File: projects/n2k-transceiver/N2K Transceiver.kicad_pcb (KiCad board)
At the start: 4 copper layers, 60 x 75 mm, 83 parts, among them J1 JTAG, SW1 SW_MEC_5G, SW2 SW_MEC_5G, SW3 SW_MEC_5G, SW4 SW_MEC_5G

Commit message: Progressing on new N2K Transceiver PCB layout
Signed-off-by: digimer <digital.mermaid@gmail.com>
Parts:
- removed C64, C65: 0.1uF, mr-stuff:Kyocera AVX 0805
- removed R24: 10kR, mr-stuff:Stackpole_RNCP1206
- removed R52: 475R, mr-stuff:Stackpole RNCP0805
- removed SW4: SW_MEC_5G, mr-stuff:SW_TS03-66-50-BK-160-LCR-D-67
- added C15: C, mr-stuff:Kyocera AVX 0805, F.Cu at (274.0, -40.7)
- added C18: C, mr-stuff:Kyocera AVX 0805, F.Cu at (230.2, -37.6)
- added C20: 0.1uF, mr-stuff:Kyocera AVX 0805, F.Cu at (125.5, 54.8)
- added C21: 0.1uF, mr-stuff:Kyocera AVX 0805, F.Cu at (172.5, 49.1)
- added C22: 0.1uF, mr-stuff:Kyocera AVX 0805, F.Cu at (172.5, 51.3)
- added C23: 0.1uF, mr-stuff:Kyocera AVX 0805, F.Cu at (172.5, 59.1)
- added C24: 0.1uF, mr-stuff:Kyocera AVX 0805, F.Cu at (172.5, 61.3)
- added C25: 0.1uF, mr-stuff:Kyocera AVX 0805, F.Cu at (205.8, 68.7)
- added C26: 0.1uF, mr-stuff:Kyocera AVX 0805, F.Cu at (205.8, 71.8)
- added C27: 0.1uF, mr-stuff:Kyocera AVX 0805, F.Cu at (205.7, 78.9)
- added C28: 0.1uF, mr-stuff:Kyocera AVX 0805, F.Cu at (205.7, 82.0)
- added C29: 0.1uF, mr-stuff:Kyocera AVX 0805, F.Cu at (205.9, 93.9)
- added C30: 0.1uF, mr-stuff:Kyocera AVX 0805, F.Cu at (205.9, 97.0)
- added C31: 0.1uF, mr-stuff:Kyocera AVX 0805, F.Cu at (205.6, 110.6)
- added HDR1: 0022112032, mr-stuff:Molex 0022112032, F.Cu at (192.5, 50.8)
- added HDR2: 0022112032, mr-stuff:Molex 0022112032, F.Cu at (192.5, 60.8)
- added HDR3: 0022112032, mr-stuff:Molex 0022112032, F.Cu at (192.5, 70.8)
- added HDR4: 0022112032, mr-stuff:Molex 0022112032, F.Cu at (192.5, 80.8)
- added HDR5: 0022112032, mr-stuff:Molex 0022112032, F.Cu at (192.5, 90.8)
- added HDR6: 0022112032, mr-stuff:Molex 0022112032, F.Cu at (192.5, 100.8)
- added HDR7: 0022112032, mr-stuff:Molex 0022112032, F.Cu at (192.5, 110.8)
- added IOX1: PI4IOE5V6416RQ2LEX, mr-stuff:Diodes Inc PI4IOE5V6416RQ2LEX, F.Cu at (249.9, 19.3)
- added R29: 475R, mr-stuff:Stackpole RNCP0805, F.Cu at (178.0, 47.1)
- added R30: 4.7kR, mr-stuff:Stackpole RMCA0805, F.Cu at (172.5, 47.1)
- added R31: 475R, mr-stuff:Stackpole RNCP0805, F.Cu at (178.0, 49.1)
- added R32: 4.7kR, mr-stuff:Stackpole RMCA0805, F.Cu at (172.5, 53.4)
- added R33: 475R, mr-stuff:Stackpole RNCP0805, F.Cu at (178.0, 57.1)
- added R34: 4.7kR, mr-stuff:Stackpole RMCA0805, F.Cu at (172.5, 57.1)
- added R35: 475R, mr-stuff:Stackpole RNCP0805, F.Cu at (178.0, 59.1)
- added R36: 4.7kR, mr-stuff:Stackpole RMCA0805, F.Cu at (172.5, 63.4)
- added R37: 475R, mr-stuff:Stackpole RNCP0805, F.Cu at (209.9, 69.3)
- added R38: 4.7kR, mr-stuff:Stackpole RMCA0805, F.Cu at (214.1, 69.1)
- added R39: 475R, mr-stuff:Stackpole RNCP0805, F.Cu at (209.8, 71.4)
- added R40: 4.7kR, mr-stuff:Stackpole RMCA0805, F.Cu at (214.1, 72.2)
- added R41: 475R, mr-stuff:Stackpole RNCP0805, F.Cu at (209.8, 79.0)
- added R42: 4.7kR, mr-stuff:Stackpole RMCA0805, F.Cu at (213.9, 79.2)
- added R43: 475R, mr-stuff:Stackpole RNCP0805, F.Cu at (209.8, 82.0)
- added R44: 4.7kR, mr-stuff:Stackpole RMCA0805, F.Cu at (213.9, 82.0)
- added R45: 475R, mr-stuff:Stackpole RNCP0805, F.Cu at (209.9, 93.9)
- added R46: 4.7kR, mr-stuff:Stackpole RMCA0805, F.Cu at (214.0, 93.9)
- added R47: 475R, mr-stuff:Stackpole RNCP0805, F.Cu at (209.9, 96.9)
- added R48: 4.7kR, mr-stuff:Stackpole RMCA0805, F.Cu at (214.0, 97.0)
- added R49: 10kR, mr-stuff:Stackpole RNCP0805, F.Cu at (234.0, -18.1)
- added R50: 10kR, mr-stuff:Stackpole RNCP0805, F.Cu at (234.0, -15.1)
- added R55: 475R, mr-stuff:Stackpole RNCP0805, F.Cu at (212.9, 110.6)
- added R57: 4.7kR, mr-stuff:Stackpole RMCA0805, F.Cu at (209.4, 110.6)
- added TVS4: TPD2E2U06QDBZRQ1, mr-stuff:TI TPD2E2U06, F.Cu at (184.0, 48.1)
- added TVS5: TPD2E2U06QDBZRQ1, mr-stuff:TI TPD2E2U06, F.Cu at (184.0, 58.1)
- added TVS6: TPD2E2U06QDBZRQ1, mr-stuff:TI TPD2E2U06, F.Cu at (201.5, 70.4)
- added TVS7: TPD2E2U06QDBZRQ1, mr-stuff:TI TPD2E2U06, F.Cu at (201.4, 80.0)
- added TVS8: TPD2E2U06QDBZRQ1, mr-stuff:TI TPD2E2U06, F.Cu at (201.5, 95.4)
- added TVS9: TPD2E2U06QDBZRQ1, mr-stuff:TI TPD2E2U06, F.Cu at (201.2, 110.6)
- C1, C12, C16, C17, C4: value 0.1uF -> C
- C10, C2, C3: value 10uF -> C
- C11, C14, C9: value 1uF -> C
- C7, C8: value 22uF -> C
- CMC1: value ACT12101012PTL00 -> ACT1210-101-2P-TL00
- H1, H2, H3, H4: value MountingHole_Pad -> MountingHole
- J1: value JTAG -> Conn_01x05_Pin
- LED1, LED2, LED3, LED4, LED5, LED6, LED7: value LED -> TLMS1101-GS15; footprint mr-stuff:ams OSRAM LS Q976.01 -> mr-stuff:Vishay TLMS1101
- R1, R10, R11, R12, R13, R17, R18, R2, R8, R9: footprint mr-stuff:Stackpole_RNCP1206 -> mr-stuff:Stackpole RNCP0805
- R14: value 15kR -> R
- R15, R16: value 5.11kR -> R
- R19, R20: value 10kR -> 4.7kR; footprint mr-stuff:Stackpole_RNCP1206 -> mr-stuff:Stackpole RMCA0805
- R3, R4, R7: value 0R -> RCA08050000ZSEASR
- R5: value 470kR -> R
- R6: value 100kR -> R
- ROM1, ROM2: value M24C64 -> STM_M24C64-RMN6P
- SD1: value VS-30MQ040HM3/5AT -> VS-30MQ040-M3_5AT
- TP1: value Comms TP -> Conn_01x10_Pin
- U1: renamed from MCU1; value ESP32-S3-WROOM-1-N16R2 -> ESP32-S3-WROOM-1; footprint mr-stuff:ESP32-S3-WROOM-1 -> RF_Module:ESP32-S3-WROOM-1
- moved REF** 302.5 mm to (386.3, 113.7)
- moved TP1 240.4 mm to (355.0, 106.8)
- moved ROM1 195.4 mm to (313.5, 77.9)
- moved ROM2 195.4 mm to (321.6, 77.9)
- moved R17 195.4 mm to (306.3, 76.3)
- moved R18 195.4 mm to (306.3, 70.5)
- moved C16 195.4 mm to (309.4, 75.9)
- moved FID3 177.3 mm to (204.4, -8.34)
- moved H3 163.0 mm to (178.6, -12.6)
- moved FID2 153.9 mm to (204.4, -11.9)
- moved R12 139.9 mm to (200.6, -22.9)
- moved H1 131.6 mm to (178.6, -32.9)
- moved R10 130.3 mm to (200.6, -29.6), turned to 0 degrees
- moved H4 127.6 mm to (178.6, -2.48)
- moved R11 126.0 mm to (200.6, -26.2), turned to 0 degrees
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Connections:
- C14 pad 1: Net-(MCU1-EN) -> Net-(U1-EN)
- C17 pad 1: GND -> +3.3V
- C17 pad 2: +3.3V -> GND
- R1 pad 1: /CAN_TX_LOCAL -> +3.3V
- R1 pad 2: +3.3V -> /CAN_TX_LOCAL
- R13 pad 1: /VBUS -> /VBUS_MCU
- R13 pad 2: /VBUS_MCU -> /VBUS
- R2 pad 1: GND -> /CAN_STANDBY
- R2 pad 2: /CAN_STANDBY -> GND
- R53 pad 2: Net-(R53-Pad2) -> Net-(C20-Pad2)
- R54 pad 2: Net-(R53-Pad2) -> Net-(C20-Pad2)
- R8 pad 1: Net-(MCU1-EN) -> +3.3V
- R8 pad 2: +3.3V -> Net-(U1-EN)
- SW1 pad 3: Net-(MCU1-EN) -> Net-(U1-EN)
- SW1 pad 4: Net-(MCU1-EN) -> Net-(U1-EN)
- SW3 pad 1: Net-(R24-Pad1) -> Net-(C20-Pad2)
- SW3 pad 2: Net-(R24-Pad1) -> Net-(C20-Pad2)
- SW3 pad 3: Net-(C64-Pad1) -> GND
- SW3 pad 4: Net-(C64-Pad1) -> GND
- TP1 pad 10: GND -> /I2C_SDA
- TP1 pad 2: /TXD0 -> GND
- TP1 pad 3: /RXD0 -> /TXD0
- TP1 pad 4: /CAN_HIGH -> /RXD0
- TP1 pad 5: /CAN_LOW -> /CAN_HIGH
- TP1 pad 6: /CAN_TX_LOCAL -> /CAN_LOW
- TP1 pad 7: /CAN_RX_LOCAL -> /CAN_TX_LOCAL
- TP1 pad 8: /I2C_SCL -> /CAN_RX_LOCAL
- TP1 pad 9: /I2C_SDA -> /I2C_SCL
- U1 pad 10: /WIFI_TX_LED -> /WIFI_RX_LED
- U1 pad 11: /WIFI_RX_LED -> /N2K_TX_LED
- U1 pad 17: /LED_ENABLE -> /LED_ENABLE_IN
- U1 pad 21: unconnected-(MCU1-IO13-Pad21) -> /IOX1_INT
- U1 pad 22: /POWER_LED -> /VBUS_MCU
- U1 pad 3: Net-(MCU1-EN) -> Net-(U1-EN)
- U1 pad 6: /N2K_TX_LED -> /POWER_LED
- U1 pad 7: /VBUS_MCU -> /WIFI_UP_LED
- U1 pad 8: /WIFI_UP_LED -> /SRV_UP_LED
- U1 pad 9: /SRV_UP_LED -> /WIFI_TX_LED
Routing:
- net /I2C_SCL: track 129.9 -> 0.00 mm, vias 3 -> 0
- net /I2C_SDA: track 115.1 -> 0.00 mm, vias 2 -> 0
- net /RXD0: track 98.0 -> 0.00 mm, vias 1 -> 0
- net /TXD0: track 94.7 -> 0.00 mm, vias 1 -> 0
- net /CAN_RX_LOCAL: track 69.7 -> 0.00 mm, vias 1 -> 0
- net /CAN_TX_LOCAL: track 70.1 -> 4.00 mm, vias 1 -> 0
- net Net-(U1-EN): track 0.00 -> 48.3 mm
- net +3.3V: track 72.6 -> 28.1 mm, vias 13 -> 10
- net /ROM2_WP: track 43.0 -> 0.00 mm, vias 4 -> 0
- net Net-(LED2-A): track 50.1 -> 10.3 mm, vias 2 -> 0
- net /ROM1_WP: track 39.8 -> 0.00 mm, vias 2 -> 0
- net Net-(LED7-A): track 47.8 -> 10.3 mm, vias 2 -> 0
- net Net-(LED3-A): track 47.5 -> 10.3 mm, vias 2 -> 0
- net Net-(LED6-A): track 47.5 -> 10.3 mm, vias 2 -> 0
- net Net-(LED5-A): track 47.2 -> 10.3 mm, vias 2 -> 0
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- added copper zone on F.Cu, net +3.3V
- removed copper zone on F.Cu, net Net-(VR1-VIN)
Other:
- board size 60 x 75 mm -> 150 x 75 mm
- board text added: "Anchor Light"
- board text added: "Beacon Mode"
- board text added: "Config"
- board text added: "Deck Light"
- board text added: "Locate Mode"
- board text added: "Off"
- board text added: "On"
- board text added: "Status LEDs"
- board text added: "Steaming Light"
- board text added: "Tricolour Light"
- board text removed: "JTAG"
- board text removed: "LEDs On"
- board text removed: "TCK"
- board text removed: "TDI"
- board text removed: "TDO"
- board text removed: "TMS"

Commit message: Finished new PCB layout
Signed-off-by: digimer <digital.mermaid@gmail.com>
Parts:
- removed J1: Conn_01x05_Pin, Connector_PinHeader_2.54mm:PinHeader_1x05_P2.54mm_Vertical
- removed U1: ESP32-S3-WROOM-1, RF_Module:ESP32-S3-WROOM-1
- added JTAG1: Conn_01x05_Pin, Connector_PinHeader_2.54mm:PinHeader_1x05_P2.54mm_Vertical, F.Cu at (195.9, 58.1)
- added MCU1: ESP32-S3-WROOM-1-N16R2, RF_Module:ESP32-S3-WROOM-1, F.Cu at (150.0, 50.0)
- added TP2: CAN Test Point, Connector_PinHeader_2.54mm:PinHeader_1x04_P2.54mm_Vertical, F.Cu at (161.2, 83.6)
- added TP3: I2C Test Point, Connector_PinHeader_2.54mm:PinHeader_1x02_P2.54mm_Vertical, F.Cu at (133.2, 65.7)
- C1, C12, C15, C16, C17, C18, C4: value C -> 0.1uF
- C10, C2, C3: value C -> 10uF
- C11, C14, C9: value C -> 1uF
- C7, C8: value C -> 22uF
- R14: value R -> 15kR; footprint mr-stuff:Stackpole_RNCP1206 -> mr-stuff:Stackpole RNCP0805
- R15, R16: value R -> 5.11kR; footprint mr-stuff:Stackpole_RNCP1206 -> mr-stuff:Stackpole RNCP0805
- R3, R4, R7: value RCA08050000ZSEASR -> 0R
- R5: value R -> 470kR
- R6: value R -> 100kR
- ROM1, ROM2: value STM_M24C64-RMN6P -> M24C64
- SD1: value VS-30MQ040-M3_5AT -> VS-30MQ040HM3/5AT
- SW1, SW2, SW3: value SW_MEC_5G -> TS03-66-50-BK-160-LCR-D-67; footprint mr-stuff:SW_TS03-66-50-BK-160-LCR-D-67 -> mr-stuff:Same Sky TS03-66
- TP1: value Conn_01x10_Pin -> Power/UART Test Point; footprint Connector_PinHeader_2.54mm:PinHeader_1x10_P2.54mm_Vertical -> Connector_PinHeader_2.54mm:PinHeader_1x04_P2.54mm_Vertical
- moved REF** 290.0 mm to (97.9, 83.6)
- moved ROM1 183.9 mm to (129.7, 72.3), turned to 0 degrees
- moved ROM2 177.0 mm to (144.7, 72.3), turned to 0 degrees
- moved C15 176.3 mm to (137.2, 70.4)
- moved R17 169.2 mm to (137.2, 72.9), turned to 180 degrees
- moved TP1 162.5 mm to (195.9, 73.9)
- moved R13 157.9 mm to (115.5, 87.4), turned to 180 degrees
- moved C16 157.3 mm to (152.2, 70.4), turned to 0 degrees
- moved R14 155.7 mm to (115.5, 89.4), turned to 180 degrees
- moved R18 154.1 mm to (152.2, 72.9), turned to 180 degrees
- moved FID3 150.3 mm to (105.4, 104.7)
- moved H3 142.1 mm to (108.5, 111.0)
- moved C18 126.1 mm to (161.9, 68.3), turned to 180 degrees
- moved R49 123.9 mm to (152.2, 75.0), turned to 180 degrees
- moved FID2 116.8 mm to (201.6, 104.9)
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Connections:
- C1 pad 1: GND -> +3.3V
- C1 pad 2: +3.3V -> GND
- C10 pad 1: GND -> +3.3V
- C10 pad 2: +3.3V -> GND
- C15 pad 1: GND -> +3.3V
- C15 pad 2: +3.3V -> GND
- C16 pad 1: GND -> +3.3V
- C16 pad 2: +3.3V -> GND
- C9 pad 1: Net-(VR1-VCC) -> GND
- C9 pad 2: GND -> Net-(VR1-VCC)
- IOX1 pad 10: /DECK_ON_IN -> /LOCATE_ON_IN
- IOX1 pad 11: /DECK_OFF_IN -> /BEACON_ON_IN
- IOX1 pad 13: /BEACON_ON_IN -> /DECK_OFF_IN
- IOX1 pad 14: /LOCATE_ON_IN -> /DECK_ON_IN
- IOX1 pad 15: unconnected-(IOX1-P1_2-Pad15) -> /STEAMING_OFF_IN
- IOX1 pad 16: unconnected-(IOX1-P1_3-Pad16) -> /STEAMING_ON_IN
- IOX1 pad 17: unconnected-(IOX1-P1_4-Pad17) -> /TRICOLOUR_OFF_IN
- IOX1 pad 18: unconnected-(IOX1-P1_5-Pad18) -> /TRICOLOUR_ON_IN
- IOX1 pad 19: unconnected-(IOX1-P1_6-Pad19) -> /ANCHOR_OFF_IN
- IOX1 pad 20: unconnected-(IOX1-P1_7-Pad20) -> /ANCHOR_ON_IN
- IOX1 pad 4: /ANCHOR_ON_IN -> unconnected-(IOX1-P0_0-Pad4)
- IOX1 pad 5: /ANCHOR_OFF_IN -> unconnected-(IOX1-P0_1-Pad5)
- IOX1 pad 6: /TRICOLOUR_ON_IN -> unconnected-(IOX1-P0_2-Pad6)
- IOX1 pad 7: /TRICOLOUR_OFF_IN -> unconnected-(IOX1-P0_3-Pad7)
- IOX1 pad 8: /STEAMING_ON_IN -> unconnected-(IOX1-P0_4-Pad8)
- IOX1 pad 9: /STEAMING_OFF_IN -> unconnected-(IOX1-P0_5-Pad9)
- R14 pad 1: GND -> /VBUS_MCU
- R14 pad 2: /VBUS_MCU -> GND
- R15 pad 1: Net-(USBRV1-CC1) -> GND
- R15 pad 2: GND -> Net-(USBRV1-CC1)
- R5 pad 1: Net-(VR1-EN) -> V_RAW
- R5 pad 2: V_RAW -> Net-(VR1-EN)
- R6 pad 1: Net-(VR1-EN) -> GND
- R6 pad 2: GND -> Net-(VR1-EN)
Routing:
- net /I2C_SDA: track 0.00 -> 107.0 mm, vias 0 -> 3
- net GND: track 111.0 -> 209.0 mm, vias 21 -> 39
- net /I2C_SCL: track 0.00 -> 97.2 mm, vias 0 -> 3
- net +3.3V: track 28.1 -> 115.8 mm, vias 10 -> 25
- net /RXD0: track 0.00 -> 76.0 mm, vias 0 -> 1
- net /TXD0: track 0.00 -> 72.3 mm, vias 0 -> 1
- net /LED_ENABLE_IN: track 0.00 -> 66.2 mm, vias 0 -> 4
- net Net-(MCU1-EN): track 48.3 -> 113.7 mm
- net /VBUS_MCU: track 0.00 -> 54.2 mm, vias 0 -> 2
- net Net-(JTAG1-Pin_5): track 0.00 -> 48.0 mm, vias 0 -> 1
- net /CAN_RX_LOCAL: track 0.00 -> 47.4 mm, vias 0 -> 3
- net Net-(JTAG1-Pin_4): track 0.00 -> 46.1 mm, vias 0 -> 1
- net Net-(JTAG1-Pin_3): track 0.00 -> 44.6 mm, vias 0 -> 1
- net /CAN_TX_LOCAL: track 4.00 -> 47.6 mm, vias 0 -> 2
- net Net-(JTAG1-Pin_2): track 0.00 -> 42.9 mm, vias 0 -> 1
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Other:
- board size 150 x 75 mm -> 100 x 72.7 mm
- board text added: "MTCK"
- board text added: "MTDI"
- board text added: "MTDO"
- board text added: "MTMS"
- board text added: "RxD0"
- board text added: "TxD0"
- board text removed: "MCU RXD0"
- board text removed: "MCU TXD0"

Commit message: Working on switching the IOX1 to the SMI1 switch chip.
Signed-off-by: digimer <digital.mermaid@gmail.com>
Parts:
- MCU1: footprint RF_Module:ESP32-S3-WROOM-1 -> mr-stuff:Espressif ESP32-S3

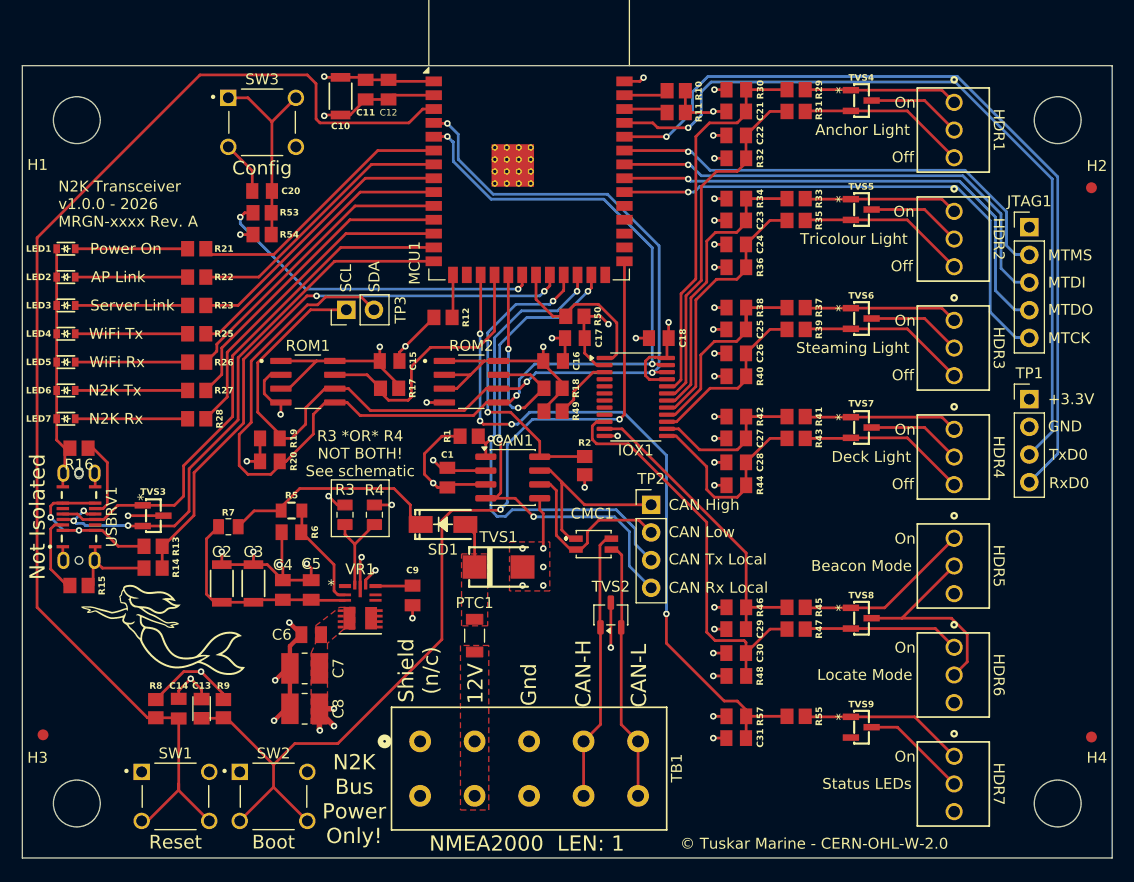
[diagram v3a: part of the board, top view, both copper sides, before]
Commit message: Added the new N2K Breakwater PCB.
This is a general purpose NMEA2000 protection board designed to be used across all projects connected to the NMEA2000 bus. It is designed to survive high voltage transients caused by conditions like an alternator dump, large inductive load transients, etc.

Signed-off-by: digimer <digital.mermaid@gmail.com>
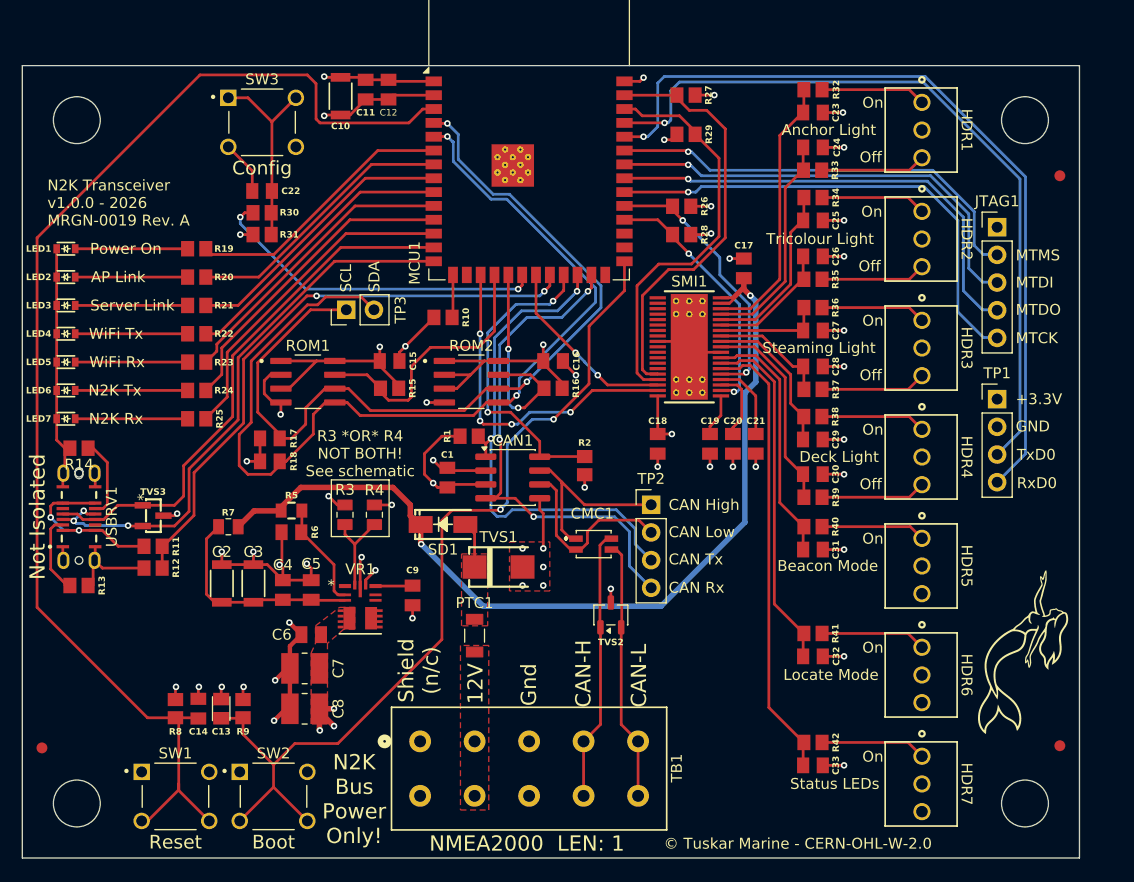
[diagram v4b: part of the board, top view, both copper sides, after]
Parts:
- removed the C23 at (169.0, 57.5)
- removed the C24 at (169.0, 59.7)
- removed IOX1: PI4IOE5V6416RQ2LEX, mr-stuff:Diodes Inc PI4IOE5V6416RQ2LEX
- removed the R10 at (163.5, 45.6)
- removed the R11 at (163.5, 47.6)
- removed the R30 at (169.0, 45.5)
- removed the R31 at (174.5, 47.5)
- removed R43, R45, R47, R55: 475R, mr-stuff:Stackpole RNCP0805
- removed R44, R46, R48, R57: 4.7kR, mr-stuff:Stackpole RMCA0805
- removed R49, R50: 10kR, mr-stuff:Stackpole RNCP0805
- removed TVS4, TVS5, TVS6, TVS7, TVS8, TVS9: TPD2E2U06QDBZRQ1, mr-stuff:TI TPD2E2U06
- added C19: 0.1uF, mr-stuff:Kyocera AVX 0805, F.Cu at (166.6, 78.0)
- added C20: 1uF, mr-stuff:Kyocera AVX 0805, F.Cu at (168.7, 78.0)
- added C21: 0.1uF, mr-stuff:Kyocera AVX 0805, F.Cu at (170.8, 78.0)
- added C32: 0.1uF, mr-stuff:Kyocera AVX 0805, F.Cu at (176.0, 97.5)
- added C33: 0.1uF, mr-stuff:Kyocera AVX 0805, F.Cu at (176.0, 107.5)
- added R26: 10kR, mr-stuff:Stackpole RNCP0805, F.Cu at (164.0, 56.2)
- added R27: 10kR, mr-stuff:Stackpole RNCP0805, F.Cu at (164.4, 46.0)
- added R28: 10kR, mr-stuff:Stackpole RNCP0805, F.Cu at (164.0, 58.8)
- added SMI1: TIC12400QDCPRQ1, mr-stuff:TI TIC12400QDCPRQ1, F.Cu at (164.7, 69.1)
- R29: value 475R -> 10kR
- R32, R34, R36, R38, R40, R42: value 4.7kR -> 100R; footprint mr-stuff:Stackpole RMCA0805 -> mr-stuff:Stackpole RNCP0805
- R33, R35, R37, R39, R41: value 475R -> 100R
- moved REF** 108.9 mm to (206.8, 78.6), turned to -90 degrees
- moved R42 30.7 mm to (176.0, 105.4)
- moved R41 20.0 mm to (176.0, 95.4)
- moved C29 18.8 mm to (176.0, 77.6), turned to 0 degrees
- moved C31 18.7 mm to (176.0, 87.7), turned to 0 degrees
- moved C30 17.9 mm to (176.0, 80.8)
- moved C17 16.8 mm to (169.7, 61.9), turned to 90 degrees
- moved R40 15.5 mm to (176.0, 85.6)
- moved R39 15.5 mm to (176.0, 82.9)
- moved C25 12.2 mm to (176.0, 57.5), turned to 0 degrees
- moved R38 12.2 mm to (176.0, 75.5)
- moved C27 12.2 mm to (176.0, 67.6), turned to 0 degrees
- moved C26 11.4 mm to (176.0, 60.8)
- moved C28 11.3 mm to (176.0, 70.9)
- moved R29 10.9 mm to (164.4, 49.6)
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- renumbered C20 to C22, C21 to C23, C22 to C24, R12 to R10, R13 to R11, R14 to R12, R15 to R13, R16 to R14, R17 to R15, R18 to R16, R19 to R17, R20 to R18, R21 to R19, R22 to R20, R23 to R21, R25 to R22, R26 to R23, R27 to R24, R28 to R25, R53 to R30, R54 to R31
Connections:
- C17 pad 1: +3.3V -> V_RAW
- C24 pad 1: GND -> /ANCHOR_OFF_IN
- C24 pad 2: /ANCHOR_OFF_IN -> GND
- C25 pad 1: /STEAMING_ON_IN -> /TRICOLOUR_ON_IN
- C26 pad 1: GND -> /TRICOLOUR_OFF_IN
- C26 pad 2: /STEAMING_OFF_IN -> GND
- C27 pad 1: /DECK_ON_IN -> /STEAMING_ON_IN
- C28 pad 1: GND -> /STEAMING_OFF_IN
- C28 pad 2: /DECK_OFF_IN -> GND
- C29 pad 1: /BEACON_ON_IN -> /DECK_ON_IN
- C30 pad 1: GND -> /DECK_OFF_IN
- C30 pad 2: /LOCATE_ON_IN -> GND
- C31 pad 1: /LED_ENABLE_IN -> /BEACON_ON_IN
- MCU1 pad 17: /LED_ENABLE_IN -> /SPI_MISO
- MCU1 pad 21: /IOX1_INT -> /SPI_MOSI
- MCU1 pad 30: unconnected-(MCU1-IO37-Pad30) -> /SMI_RESET
- MCU1 pad 31: unconnected-(MCU1-IO38-Pad31) -> /SMI_INT
- MCU1 pad 38: Net-(MCU1-IO2) -> /SPI_CLK
- MCU1 pad 39: Net-(MCU1-IO1) -> /SPI_CS
- R29 pad 1: /ANCHOR_ON_PLUG -> /SPI_CLK
- R29 pad 2: /ANCHOR_ON_IN -> GND
- R32 pad 1: /ANCHOR_OFF_IN -> /ANCHOR_ON_PLUG
- R32 pad 2: +3.3V -> /ANCHOR_ON_IN
- R33 pad 1: /TRICOLOUR_ON_PLUG -> /ANCHOR_OFF_PLUG
- R33 pad 2: /TRICOLOUR_ON_IN -> /ANCHOR_OFF_IN
- R34 pad 1: /TRICOLOUR_ON_IN -> /TRICOLOUR_ON_PLUG
- R34 pad 2: +3.3V -> /TRICOLOUR_ON_IN
- R36 pad 1: /TRICOLOUR_OFF_IN -> /STEAMING_ON_PLUG
- R36 pad 2: +3.3V -> /STEAMING_ON_IN
- R37 pad 1: /STEAMING_ON_PLUG -> /STEAMING_OFF_PLUG
- R37 pad 2: /STEAMING_ON_IN -> /STEAMING_OFF_IN
- R38 pad 1: /STEAMING_ON_IN -> /DECK_ON_PLUG
- R38 pad 2: +3.3V -> /DECK_ON_IN
- R39 pad 1: /STEAMING_OFF_PLUG -> /DECK_OFF_PLUG
- R39 pad 2: /STEAMING_OFF_IN -> /DECK_OFF_IN
- R40 pad 1: /STEAMING_OFF_IN -> /BEACON_ON_PLUG
- R40 pad 2: +3.3V -> /BEACON_ON_IN
- R41 pad 1: /DECK_ON_PLUG -> /LOCATE_ON_PLUG
- R41 pad 2: /DECK_ON_IN -> /LOCATE_ON_IN
- R42 pad 1: /DECK_ON_IN -> /LED_ENABLE_PLUG
- R42 pad 2: +3.3V -> /LED_ENABLE_IN
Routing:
- net V_RAW: track 20.3 -> 87.0 mm, vias 0 -> 2
- net GND: track 209.0 -> 152.8 mm, vias 39 -> 45
- net /SPI_CS: track 0.00 -> 38.9 mm
- net /SPI_CLK: track 0.00 -> 37.4 mm
- net /SPI_MISO: track 0.00 -> 31.3 mm, vias 0 -> 4
- net +3.3V: track 115.8 -> 85.9 mm, vias 25 -> 16
- net /SMI_INT: track 0.00 -> 25.1 mm, vias 0 -> 2
- net /LED_ENABLE_IN: track 66.2 -> 41.6 mm, vias 4 -> 0
- net /SMI_RESET: track 0.00 -> 23.6 mm, vias 0 -> 2
- net /SPI_MOSI: track 0.00 -> 17.4 mm, vias 0 -> 2
- net /I2C_SCL: track 97.2 -> 79.8 mm, vias 3 -> 2
- net /I2C_SDA: track 107.0 -> 89.8 mm, vias 3 -> 2
- net /IOX1_INT: track 15.7 -> 0.00 mm
- net /ANCHOR_OFF_IN: track 32.9 -> 20.2 mm
- net /TRICOLOUR_OFF_IN: track 24.2 -> 11.6 mm
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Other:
- board size 100 x 72.7 mm -> 97 x 72.7 mm
- board text added: "CAN Rx"
- board text added: "CAN Tx"
- board text added: "N2K Transceiver v1.0.0 - 2026 MRGN-0019 Rev. A"
- board text removed: "CAN Rx Local"
- board text removed: "CAN Tx Local"
- board text removed: "N2K Transceiver v1.0.0 - 2026 MRGN-xxxx Rev. A"
